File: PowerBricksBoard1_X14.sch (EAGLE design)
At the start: 16 parts

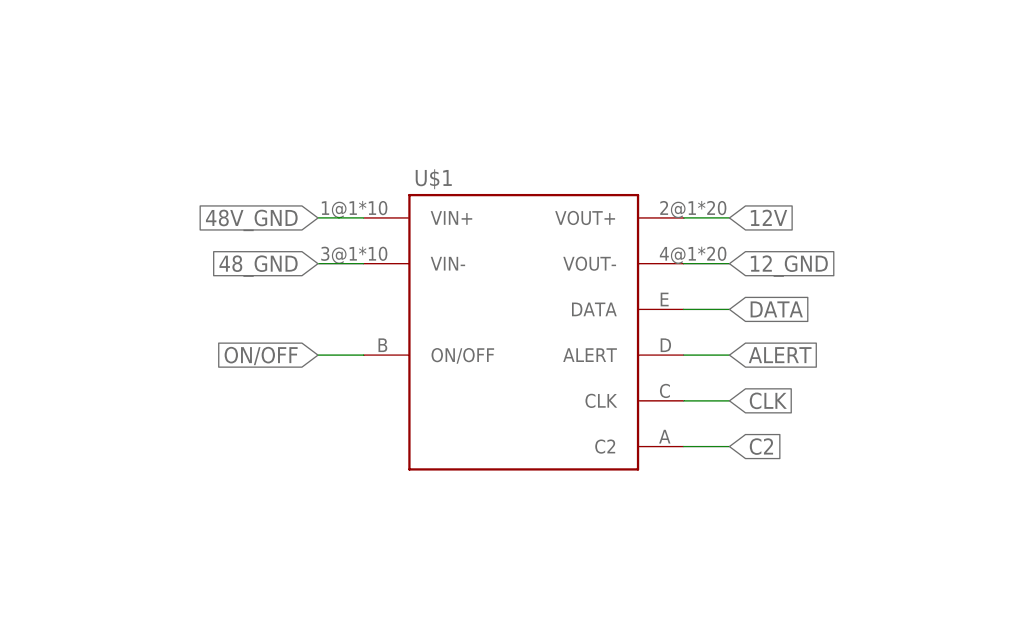
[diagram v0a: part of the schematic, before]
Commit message: imported new connector into drawing
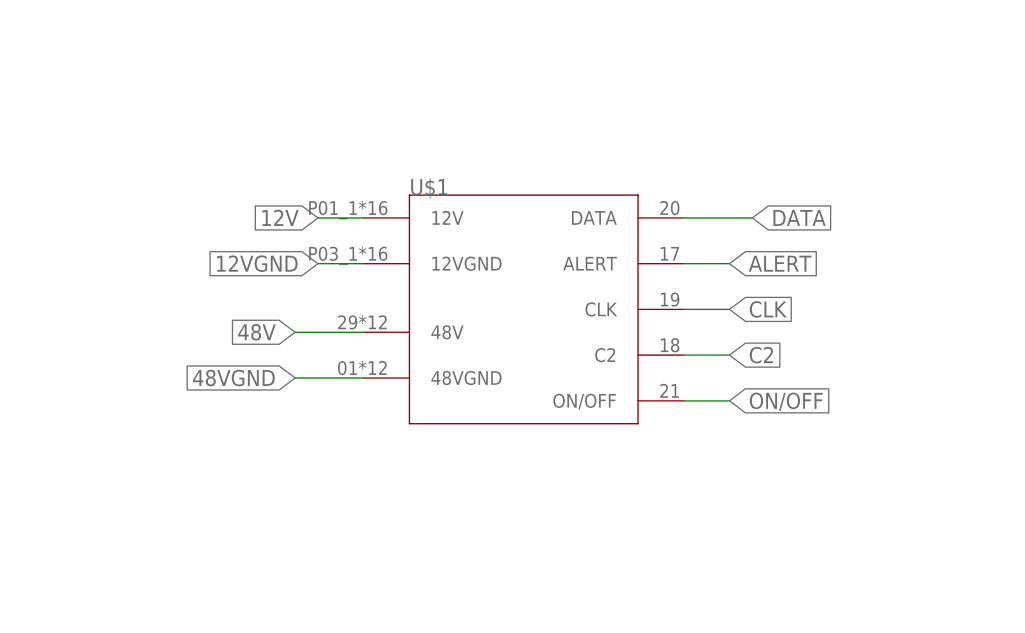
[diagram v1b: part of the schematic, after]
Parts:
- U$1: value BRICK2DIST -> PETC-02-40-01-X-VT(BTOD); device Brick_Dist_Connector:BRICK2DIST -> CONN, Distribution-Bricks:PETC-02-40-01-X-VT(BTOD)
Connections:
- new net 12VGND: U$1.12VGND
- new net 48VGND: U$1.48VGND
- net 12V: now also U$1.12V; no longer U$1.VOUT+
- net 12_GND: no longer U$1.VOUT-
- net 48V: now also U$1.48V
- net 48V_GND: no longer U$1.VIN+
- net 48_GND: no longer U$1.VIN-
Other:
- moved on the sheet: U$1
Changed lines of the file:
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@@
 <part name="R3" library="SparkFun-Resistors" library_urn="urn:adsk.eagle:library:532" deviceset="RESISTOR" device="0603" package3d_urn="urn:adsk.eagle:package:39650/1" value=" "/>
 <part name="R5" library="SparkFun-Resistors" library_urn="urn:adsk.eagle:library:532" deviceset="RESISTOR" device="0603" package3d_urn="urn:adsk.eagle:package:39650/1" value="510k"/>
-<part name="U$1" library="Brick_Dist_Connector" deviceset="BRICK2DIST" device=""/>
+<part name="U$1" library="CONN, Distribution-Bricks" deviceset="PETC-02-40-01-X-VT(BTOD)" device=""/>
 </parts>
 <sheets>
@@
 <attribute name="VALUE" x="109.22" y="115.316" size="1.778" layer="96" font="vector" align="top-center"/>
 </instance>
-<instance part="U$1" gate="G$1" x="182.88" y="124.46" smashed="yes">
-<attribute name="NAME" x="183.388" y="133.096" size="1.778" layer="95"/>
+<instance part="U$1" gate="G$1" x="195.58" y="119.38" smashed="yes">
+<attribute name="NAME" x="182.88" y="132.08" size="1.778" layer="95"/>
 </instance>
 </instances>
@@
 <nets>
 <net name="48V_GND" class="0">
-<segment>
-<wire x1="177.8" y1="129.54" x2="172.72" y2="129.54" width="0.1524" layer="91"/>
-<label x="172.72" y="129.54" size="1.778" layer="95" rot="R180" xref="yes"/>
-<pinref part="U$1" gate="G$1" pin="VIN+"/>
-</segment>
 <segment>
 <wire x1="60.96" y1="127" x2="55.88" y2="127" width="0.1524" layer="91"/>
@@
 </segment>
 <segment>
-<wire x1="177.8" y1="124.46" x2="172.72" y2="124.46" width="0.1524" layer="91"/>
-<label x="172.72" y="124.46" size="1.778" layer="95" rot="R180" xref="yes"/>
-<pinref part="U$1" gate="G$1" pin="VIN-"/>
-</segment>
-<segment>
 <wire x1="60.96" y1="99.06" x2="55.88" y2="99.06" width="0.1524" layer="91"/>
 <label x="55.88" y="99.06" size="1.778" layer="95" rot="R180" xref="yes"/>
@@
 <wire x1="99.06" y1="48.26" x2="99.06" y2="53.34" width="0.1524" layer="91"/>
 <label x="99.06" y="53.34" size="1.778" layer="95" rot="R90" xref="yes"/>
-</segment>
-<segment>
-<wire x1="213.36" y1="129.54" x2="218.44" y2="129.54" width="0.1524" layer="91"/>
-<label x="218.44" y="129.54" size="1.778" layer="95" xref="yes"/>
-<pinref part="U$1" gate="G$1" pin="VOUT+"/>
 </segment>
 <segment>
@@
 <junction x="104.14" y="127"/>
 </segment>
+<segment>
+<wire x1="177.8" y1="129.54" x2="172.72" y2="129.54" width="0.1524" layer="91"/>
+<label x="172.72" y="129.54" size="1.778" layer="95" rot="R180" xref="yes"/>
+<pinref part="U$1" gate="G$1" pin="12V"/>
+</segment>
 </net>
 <net name="C2" class="0">
-<segment>
-<wire x1="213.36" y1="104.14" x2="218.44" y2="104.14" width="0.1524" layer="91"/>
-<label x="218.44" y="104.14" size="1.778" layer="95" xref="yes"/>
-<pinref part="U$1" gate="G$1" pin="C2"/>
-</segment>
 <segment>
 <wire x1="96.52" y1="111.76" x2="104.14" y2="111.76" width="0.1524" layer="91"/>
@@
 <pinref part="U$2" gate="G$1" pin="C2"/>
 </segment>
+<segment>
+<wire x1="213.36" y1="114.3" x2="218.44" y2="114.3" width="0.1524" layer="91"/>
+<label x="218.44" y="114.3" size="1.778" layer="95" xref="yes"/>
+<pinref part="U$1" gate="G$1" pin="C2"/>
+</segment>
 </net>
 <net name="12_GND" class="0">
@@
 <wire x1="99.06" y1="27.94" x2="99.06" y2="22.86" width="0.1524" layer="91"/>
 <label x="99.06" y="22.86" size="1.778" layer="95" rot="R270" xref="yes"/>
-</segment>
-<segment>
-<wire x1="213.36" y1="124.46" x2="218.44" y2="124.46" width="0.1524" layer="91"/>
-<label x="218.44" y="124.46" size="1.778" layer="95" xref="yes"/>
-<pinref part="U$1" gate="G$1" pin="VOUT-"/>
 </segment>
 <segment>
@@
 <net name="ALERT" class="0">
 <segment>
-<wire x1="213.36" y1="114.3" x2="218.44" y2="114.3" width="0.1524" layer="91"/>
-<label x="218.44" y="114.3" size="1.778" layer="95" xref="yes"/>
-<pinref part="U$1" gate="G$1" pin="ALERT"/>
-</segment>
-<segment>
 <wire x1="60.96" y1="109.22" x2="55.88" y2="109.22" width="0.1524" layer="91"/>
 <label x="55.88" y="109.22" size="1.778" layer="95" rot="R180" xref="yes"/>
 <pinref part="U$2" gate="G$1" pin="SMBALERT"/>
 </segment>
+<segment>
+<wire x1="213.36" y1="124.46" x2="218.44" y2="124.46" width="0.1524" layer="91"/>
+<label x="218.44" y="124.46" size="1.778" layer="95" xref="yes"/>
+<pinref part="U$1" gate="G$1" pin="ALERT"/>
+</segment>
 </net>
 <net name="DATA" class="0">
-<segment>
-<wire x1="213.36" y1="119.38" x2="218.44" y2="119.38" width="0.1524" layer="91"/>
-<label x="218.44" y="119.38" size="1.778" layer="95" xref="yes"/>
-<pinref part="U$1" gate="G$1" pin="DATA"/>
-</segment>
 <segment>
 <wire x1="60.96" y1="104.14" x2="35.56" y2="104.14" width="0.1524" layer="91"/>
@@
 <pinref part="U$2" gate="G$1" pin="PMBDATA"/>
 </segment>
+<segment>
+<wire x1="213.36" y1="129.54" x2="220.98" y2="129.54" width="0.1524" layer="91"/>
+<label x="220.98" y="129.54" size="1.778" layer="95" xref="yes"/>
+<pinref part="U$1" gate="G$1" pin="DATA"/>
+</segment>
 </net>
 <net name="CLK" class="0">
-<segment>
-<wire x1="213.36" y1="109.22" x2="218.44" y2="109.22" width="0.1524" layer="91"/>
-<label x="218.44" y="109.22" size="1.778" layer="95" xref="yes"/>
-<pinref part="U$1" gate="G$1" pin="CLK"/>
-</segment>
 <segment>
 <wire x1="60.96" y1="106.68" x2="44.196" y2="106.68" width="0.1524" layer="91"/>
 <label x="44.196" y="106.68" size="1.778" layer="95" rot="R180" xref="yes"/>
 <pinref part="U$2" gate="G$1" pin="PMBCLK"/>
+</segment>
+<segment>
+<wire x1="213.36" y1="119.38" x2="218.44" y2="119.38" width="0.1524" layer="91"/>
+<label x="218.44" y="119.38" size="1.778" layer="95" xref="yes"/>
+<pinref part="U$1" gate="G$1" pin="CLK"/>
 </segment>
 </net>
@@
 </segment>
 <segment>
-<wire x1="177.8" y1="114.3" x2="172.72" y2="114.3" width="0.1524" layer="91"/>
-<label x="172.72" y="114.3" size="1.778" layer="95" rot="R180" xref="yes"/>
+<wire x1="213.36" y1="109.22" x2="218.44" y2="109.22" width="0.1524" layer="91"/>
+<label x="218.44" y="109.22" size="1.778" layer="95" xref="yes"/>
 <pinref part="U$1" gate="G$1" pin="ON/OFF"/>
 </segment>
@@
 <wire x1="66.04" y1="48.26" x2="66.04" y2="40.64" width="0.1524" layer="91"/>
 </segment>
-</net>
+<segment>
+<pinref part="U$1" gate="G$1" pin="48V"/>
+<wire x1="177.8" y1="116.84" x2="170.18" y2="116.84" width="0.1524" layer="91"/>
+<label x="170.18" y="116.84" size="1.778" layer="95" rot="MR0" xref="yes"/>
+</segment>
+</net>
+<net name="12VGND" class="0">
+<segment>
+<wire x1="177.8" y1="124.46" x2="172.72" y2="124.46" width="0.1524" layer="91"/>
+<label x="172.72" y="124.46" size="1.778" layer="95" rot="R180" xref="yes"/>
+<pinref part="U$1" gate="G$1" pin="12VGND"/>
+</segment>
+</net>
+<net name="48VGND" class="0">
+<segment>
+<pinref part="U$1" gate="G$1" pin="48VGND"/>
+<wire x1="177.8" y1="111.76" x2="170.18" y2="111.76" width="0.1524" layer="91"/>
+<label x="170.18" y="111.76" size="1.778" layer="95" rot="MR0" xref="yes"/>
+</segment>
+</net>

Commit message: update
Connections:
- removed net 48V_GND: U$2.VIN(+)
- net 48V: now also U$2.VIN(+)
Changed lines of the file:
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@@
 </busses>
 <nets>
-<net name="48V_GND" class="0">
-<segment>
-<wire x1="60.96" y1="127" x2="55.88" y2="127" width="0.1524" layer="91"/>
-<label x="55.88" y="127" size="1.778" layer="95" rot="R180" xref="yes"/>
-<pinref part="U$2" gate="G$1" pin="VIN(+)"/>
-</segment>
-</net>
 <net name="48_GND" class="0">
 <segment>
@@
 <label x="170.18" y="116.84" size="1.778" layer="95" rot="MR0" xref="yes"/>
 </segment>
-</net>
+<segment>
+<pinref part="U$2" gate="G$1" pin="VIN(+)"/>
+<wire x1="60.96" y1="127" x2="55.88" y2="127" width="0.1524" layer="91"/>
+<label x="55.88" y="127" size="1.778" layer="95" rot="R180" xref="yes"/>
+</segment>
+</net>

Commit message: I deleted the old board and made a new one with the connector type.
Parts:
- U$1: value PETC-02-40-01-X-VT(BTOD) -> CONN_BRICKS; device CONN, Distribution-Bricks:PETC-02-40-01-X-VT(BTOD) -> CONN, Distribution-Bricks:CONN_BRICKS
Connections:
- removed net 48VGND: U$1.48VGND
- net 48_GND: now also U$1.48VGND
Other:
- moved on the sheet: U$1
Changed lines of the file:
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@@
 <part name="R3" library="SparkFun-Resistors" library_urn="urn:adsk.eagle:library:532" deviceset="RESISTOR" device="0603" package3d_urn="urn:adsk.eagle:package:39650/1" value=" "/>
 <part name="R5" library="SparkFun-Resistors" library_urn="urn:adsk.eagle:library:532" deviceset="RESISTOR" device="0603" package3d_urn="urn:adsk.eagle:package:39650/1" value="510k"/>
-<part name="U$1" library="CONN, Distribution-Bricks" deviceset="PETC-02-40-01-X-VT(BTOD)" device=""/>
+<part name="U$1" library="CONN, Distribution-Bricks" deviceset="CONN_BRICKS" device=""/>
 </parts>
 <sheets>
@@
 <pinref part="U$2" gate="G$1" pin="VIN(-)"/>
 </segment>
+<segment>
+<wire x1="177.8" y1="111.76" x2="170.18" y2="111.76" width="0.1524" layer="91"/>
+<label x="170.18" y="111.76" size="1.778" layer="95" rot="MR0" xref="yes"/>
+<pinref part="U$1" gate="G$1" pin="48VGND"/>
+</segment>
 </net>
 <net name="12V" class="0">
@@
 </segment>
 <segment>
-<pinref part="U$1" gate="G$1" pin="48V"/>
 <wire x1="177.8" y1="116.84" x2="170.18" y2="116.84" width="0.1524" layer="91"/>
 <label x="170.18" y="116.84" size="1.778" layer="95" rot="MR0" xref="yes"/>
+<pinref part="U$1" gate="G$1" pin="48V"/>
 </segment>
 <segment>
@@
 </segment>
 </net>
-<net name="48VGND" class="0">
-<segment>
-<pinref part="U$1" gate="G$1" pin="48VGND"/>
-<wire x1="177.8" y1="111.76" x2="170.18" y2="111.76" width="0.1524" layer="91"/>
-<label x="170.18" y="111.76" size="1.778" layer="95" rot="MR0" xref="yes"/>
-</segment>
-</net>

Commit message: Needed a design review and some bugs
DRC keepings giving me polygon priority issues
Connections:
- removed net 12VGND: U$1.12VGND
- net 12_GND: now also U$1.12VGND
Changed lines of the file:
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@@
 <pinref part="U$2" gate="G$1" pin="SENSE(-)"/>
+</segment>
+<segment>
+<wire x1="177.8" y1="124.46" x2="172.72" y2="124.46" width="0.1524" layer="91"/>
+<label x="172.72" y="124.46" size="1.778" layer="95" rot="R180" xref="yes"/>
+<pinref part="U$1" gate="G$1" pin="12VGND"/>
 </segment>
 </net>
@@
 </segment>
 </net>
-<net name="12VGND" class="0">
-<segment>
-<wire x1="177.8" y1="124.46" x2="172.72" y2="124.46" width="0.1524" layer="91"/>
-<label x="172.72" y="124.46" size="1.778" layer="95" rot="R180" xref="yes"/>
-<pinref part="U$1" gate="G$1" pin="12VGND"/>
-</segment>
-</net>

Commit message: dsss
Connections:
- net ALERT: now also U$1.C2; no longer U$1.ALERT
- net C2: now also U$1.DATA; no longer U$1.C2
- net DATA: now also U$1.ALERT; no longer U$1.DATA
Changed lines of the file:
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@@
 </segment>
 <segment>
-<wire x1="213.36" y1="114.3" x2="218.44" y2="114.3" width="0.1524" layer="91"/>
-<label x="218.44" y="114.3" size="1.778" layer="95" xref="yes"/>
-<pinref part="U$1" gate="G$1" pin="C2"/>
+<wire x1="213.36" y1="129.54" x2="220.98" y2="129.54" width="0.1524" layer="91"/>
+<label x="220.98" y="129.54" size="1.778" layer="95" xref="yes"/>
+<pinref part="U$1" gate="G$1" pin="DATA"/>
 </segment>
 </net>
@@
 </segment>
 <segment>
-<wire x1="213.36" y1="124.46" x2="218.44" y2="124.46" width="0.1524" layer="91"/>
-<label x="218.44" y="124.46" size="1.778" layer="95" xref="yes"/>
-<pinref part="U$1" gate="G$1" pin="ALERT"/>
+<wire x1="213.36" y1="114.3" x2="218.44" y2="114.3" width="0.1524" layer="91"/>
+<label x="218.44" y="114.3" size="1.778" layer="95" xref="yes"/>
+<pinref part="U$1" gate="G$1" pin="C2"/>
 </segment>
 </net>
@@
 </segment>
 <segment>
-<wire x1="213.36" y1="129.54" x2="220.98" y2="129.54" width="0.1524" layer="91"/>
-<label x="220.98" y="129.54" size="1.778" layer="95" xref="yes"/>
-<pinref part="U$1" gate="G$1" pin="DATA"/>
+<wire x1="213.36" y1="124.46" x2="218.44" y2="124.46" width="0.1524" layer="91"/>
+<label x="218.44" y="124.46" size="1.778" layer="95" xref="yes"/>
+<pinref part="U$1" gate="G$1" pin="ALERT"/>
 </segment>
 </net>
